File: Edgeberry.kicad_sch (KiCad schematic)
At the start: 27 parts, among them P1 12Vin, Q1 BC547, Q2 BC547, Q3 BC547, SW1 SW_PUSH, U1 24LC256, U2 LM2596S-5.0

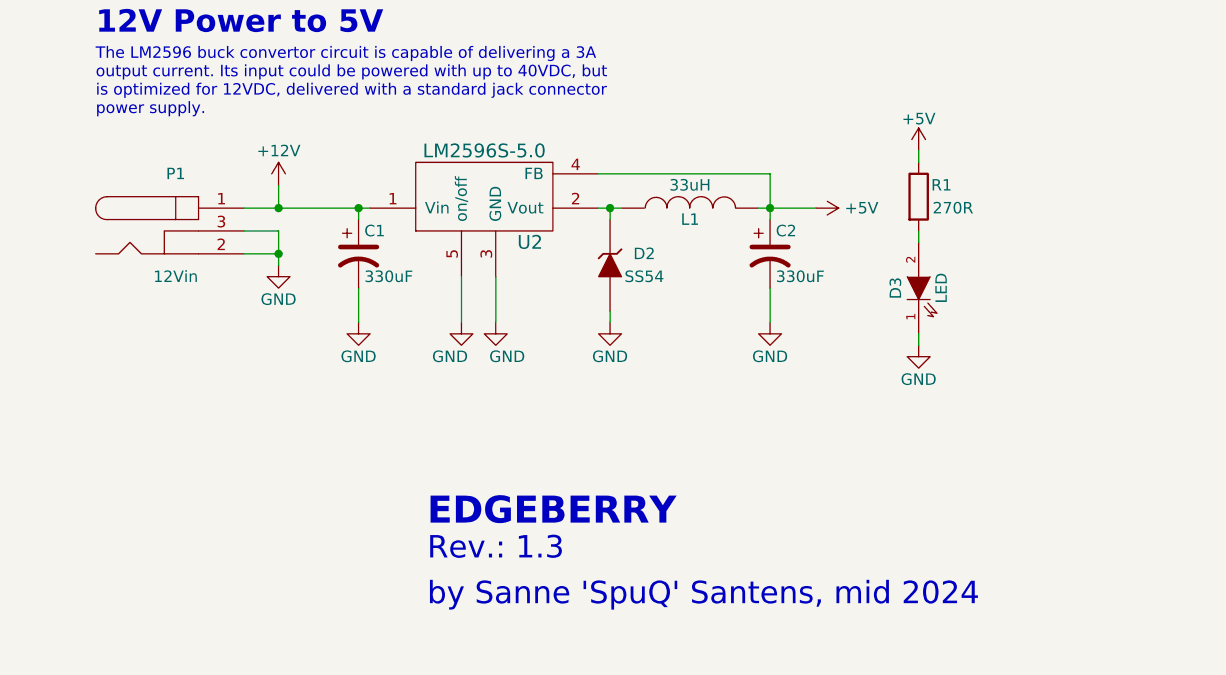
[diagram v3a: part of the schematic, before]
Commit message: Added a Molex 2Pin header on 12V
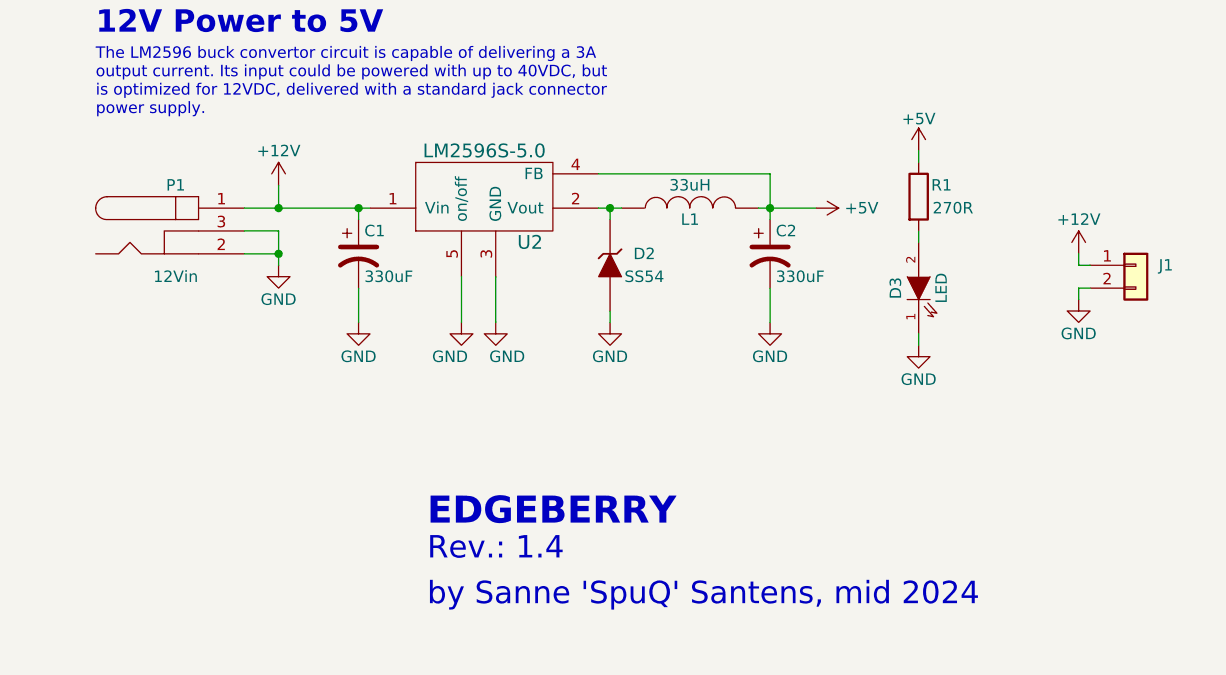
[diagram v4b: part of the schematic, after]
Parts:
- added J1: Molex_KK_1x02_P2.54mm, Connector_Molex:Molex_KK-254_AE-6410-02A_1x02_P2.54mm_Vertical, symbol Connector_Generic:Conn_01x02
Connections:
- net +12V: now also J1.1 (Pin_1)
- net GND: now also J1.2 (Pin_2)
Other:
- note added: "Rev.: 1.4"
- note removed: "Rev.: 1.3"
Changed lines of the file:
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@@
     (title "Edgeberry Hardware")
     (date "2024-05-15")
-    (rev "1.3")
+    (rev "1.4")
   )
   (junction (at 91.44 149.86) (diameter 0) (color 0 0 0 0)
@@
     (stroke (width 0) (type default) (color 0 0 0 0))
   )
+  (wire (pts (xy 255.27 142.24) (xy 254 142.24))
+    (stroke (width 0) (type default) (color 0 0 0 0))
+  )
   (wire (pts (xy 58.42 148.59) (xy 58.42 149.86))
     (stroke (width 0) (type default) (color 0 0 0 0))
@@
     (stroke (width 0) (type default) (color 0 0 0 0))
   )
+  (wire (pts (xy 254 144.78) (xy 254 146.05))
+    (stroke (width 0) (type default) (color 0 0 0 0))
+  )
   (wire (pts (xy 130.81 39.37) (xy 133.35 39.37))
     (stroke (width 0) (type default) (color 0 0 0 0))
@@
     (stroke (width 0) (type default) (color 0 0 0 0))
   )
+  (wire (pts (xy 255.27 144.78) (xy 254 144.78))
+    (stroke (width 0) (type default) (color 0 0 0 0))
+  )
   (wire (pts (xy 201.93 135.89) (xy 203.2 135.89))
     (stroke (width 0) (type default) (color 0 0 0 0))
@@
   )
   (wire (pts (xy 130.81 64.77) (xy 133.35 64.77))
+    (stroke (width 0) (type default) (color 0 0 0 0))
+  )
+  (wire (pts (xy 254 142.24) (xy 254 140.97))
     (stroke (width 0) (type default) (color 0 0 0 0))
   )
@@
     (effects (font (size 1.27 1.27)) (justify left bottom))
   )
-  (text "Rev.: 1.3" (at 181.61 175.26 0)
+  (text "Rev.: 1.4" (at 181.61 175.26 0)
     (effects (font (size 2.4892 2.4892)) (justify left bottom))
   )
@@
   (symbol (lib_id "EdgeBerry-rescue:BARREL_JACK") (at 153.67 138.43 0) (unit 1)
     (in_bom yes) (on_board yes)
-    (property "Reference" "P1" (id 0) (at 153.67 132.08 0))
+    (property "Reference" "P1" (id 0) (at 153.67 133.35 0))
     (property "Value" "12Vin" (id 1) (at 153.67 143.51 0))
     (property "Footprint" "Connector_BarrelJack:BarrelJack_Horizontal" (id 2) (at 153.67 138.43 0)
@@
     (pin "1")
   )
+  (symbol (lib_id "power:+12V") (at 254 140.97 0) (unit 1)
+    (in_bom yes) (on_board yes)
+    (property "Reference" "#PWR0106" (id 0) (at 254 144.78 0)
+      (effects (font (size 1.27 1.27)) hide)
+    )
+    (property "Value" "+12V" (id 1) (at 254 137.16 0))
+    (property "Footprint" "" (id 2) (at 254 140.97 0)
+      (effects (font (size 1.27 1.27)) hide)
+    )
+    (property "Datasheet" "" (id 3) (at 254 140.97 0)
+      (effects (font (size 1.27 1.27)) hide)
+    )
+    (pin "1")
+  )
   (symbol (lib_id "EdgeBerry-rescue:+3V3") (at 130.81 34.29 90) (unit 1)
     (in_bom yes) (on_board yes)
-    (property "Reference" "#PWR?" (id 0) (at 134.62 34.29 0)
+    (property "Reference" "#PWR0107" (id 0) (at 134.62 34.29 0)
       (effects (font (size 1.27 1.27)) hide)
     )
@@
     (pin "1")
   )
+  (symbol (lib_id "Connector_Generic:Conn_01x02") (at 260.35 142.24 0) (unit 1)
+    (in_bom yes) (on_board yes)
+    (property "Reference" "J1" (id 0) (at 262.89 142.2399 0)
+      (effects (font (size 1.27 1.27)) (justify left))
+    )
+    (property "Value" "Molex_KK_1x02_P2.54mm" (id 1) (at 256.54 147.32 0)
+      (effects (font (size 1.27 1.27)) (justify left) hide)
+    )
+    (property "Footprint" "Connector_Molex:Molex_KK-254_AE-6410-02A_1x02_P2.54mm_Vertical" (id 2) (at 260.35 142.24 0)
+      (effects (font (size 1.27 1.27)) hide)
+    )
+    (property "Datasheet" "~" (id 3) (at 260.35 142.24 0)
+      (effects (font (size 1.27 1.27)) hide)
+    )
+    (pin "1")
+    (pin "2")
+  )
   (symbol (lib_id "power:+5V") (at 54.61 29.21 0) (unit 1)
     (in_bom yes) (on_board yes)
@@
     (pin "2")
   )
+  (symbol (lib_id "power:GND") (at 254 146.05 0) (unit 1)
+    (in_bom yes) (on_board yes)
+    (property "Reference" "#PWR0105" (id 0) (at 254 152.4 0)
+      (effects (font (size 1.27 1.27)) hide)
+    )
+    (property "Value" "GND" (id 1) (at 254 149.86 0))
+    (property "Footprint" "" (id 2) (at 254 146.05 0)
+      (effects (font (size 1.27 1.27)) hide)
+    )
+    (property "Datasheet" "" (id 3) (at 254 146.05 0)
+      (effects (font (size 1.27 1.27)) hide)
+    )
+    (pin "1")
+  )
   (sheet_instances
     (path "/" (page "1"))
@@
       (reference "#PWR0103") (unit 1) (value "+5V") (footprint "")
     )
-    (path "/1eae0866-fb43-460e-ba70-4206816f3ae0"
+    (path "/1eae0866-fb43-460e-ba70-4206816f3ae1"
       (reference "#PWR0104") (unit 1) (value "+5V") (footprint "")
     )
+    (path "/f44cc862-d425-4144-8846-d84278a3c917"
+      (reference "#PWR0105") (unit 1) (value "GND") (footprint "")
+    )
+    (path "/2623d6cf-f221-488b-8577-990bdece26e9"
+      (reference "#PWR0106") (unit 1) (value "+12V") (footprint "")
+    )
     (path "/59ba752a-b2a2-4535-9bd8-a06a7b8b7a31"
-      (reference "#PWR?") (unit 1) (value "+3V3") (footprint "")
+      (reference "#PWR0107") (unit 1) (value "+3V3") (footprint "")
     )
     (path "/00000000-0000-0000-0000-00005b755152"
@@
       (reference "H1") (unit 1) (value "EdgeBerry_IO") (footprint "emcosys:EdgeBerry_IO")
     )
+    (path "/8a9dd820-4ec5-4959-94a2-489c1e5fdf0f"
+      (reference "J1") (unit 1) (value "Molex_KK_1x02_P2.54mm") (footprint "Connector_Molex:Molex_KK-254_AE-6410-02A_1x02_P2.54mm_Vertical")
+    )
     (path "/0a17adb6-bec6-42e3-96c1-992b250e6557"

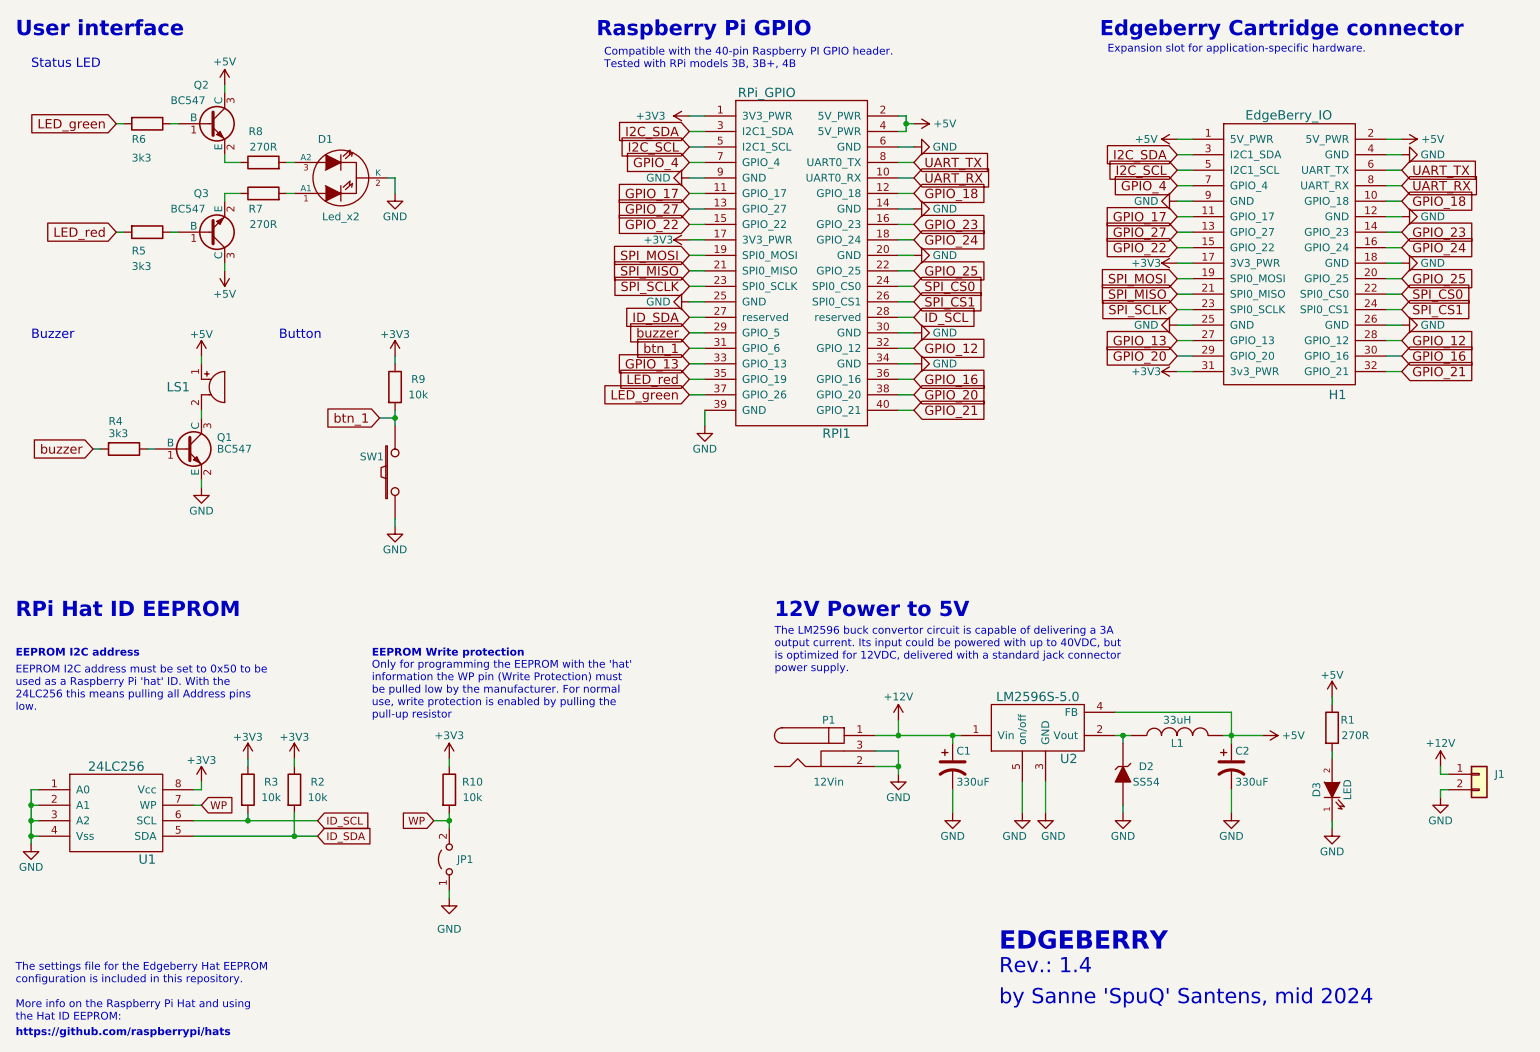
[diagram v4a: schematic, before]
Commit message: Bugfix RPi footprint + via's are via's now instead footprints. KiCad * update.
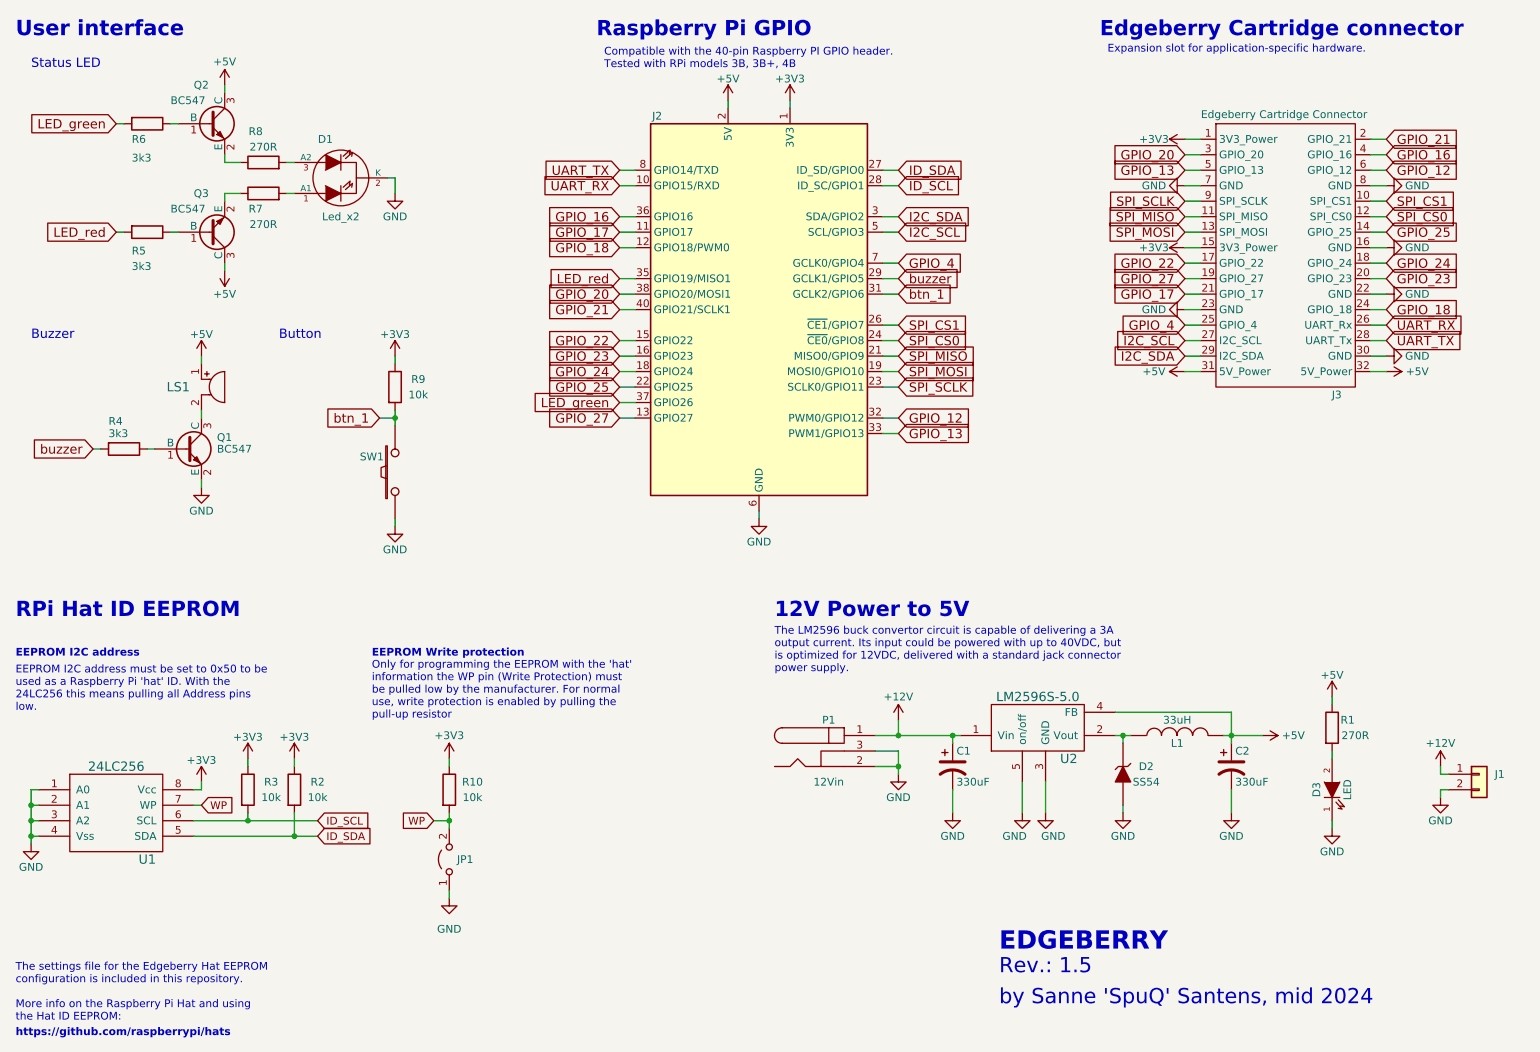
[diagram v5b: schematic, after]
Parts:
- removed H1: EdgeBerry_IO, emcosys:EdgeBerry_IO, symbol EdgeBerry-rescue:EdgeBerry_IO
- removed RPI1: RPi_GPIO, emcosys:RPI_GPIO, symbol EdgeBerry-rescue:RPi_GPIO
- added J2: Raspberry_Pi_2_3, Connector_PinSocket_2.54mm:PinSocket_2x20_P2.54mm_Vertical, symbol Connector:Raspberry_Pi_2_3
- added J3: Edgeberry Cartridge Connector, Connector_PinSocket_2.54mm:PinSocket_2x16_P2.54mm_Horizontal, symbol Edgeberry:Edgeberry_Cartridge_Connector
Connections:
- net +3V3: now also J2.1 (3V3), J2.17 (3V3), J3.1 (3V3_Power), J3.15 (3V3_Power)
- net +5V: now also J2.2 (5V), J2.4 (5V), J3.31 (5V_Power), J3.32 (5V_Power)
- net GND: now also J2.14 (GND), J2.20 (GND), J2.25 (GND), J2.30 (GND), J2.34 (GND), J2.39 (GND), J2.6 (GND), J2.9 (GND), J3.16 (GND), J3.22 (GND), J3.23 (GND), J3.30 (GND), J3.7 (GND), J3.8 (GND)
- net GPIO_12: now also J2.32 (PWM0/GPIO12), J3.6 (GPIO_12)
- net GPIO_13: now also J2.33 (PWM1/GPIO13), J3.5 (GPIO_13)
- net GPIO_16: now also J2.36 (GPIO16), J3.4 (GPIO_16)
- net GPIO_17: now also J2.11 (GPIO17), J3.21 (GPIO_17)
- net GPIO_18: now also J2.12 (GPIO18/PWM0), J3.24 (GPIO_18)
- net GPIO_20: now also J2.38 (GPIO20/MOSI1), J3.3 (GPIO_20)
- net GPIO_21: now also J2.40 (GPIO21/SCLK1), J3.2 (GPIO_21)
- net GPIO_22: now also J2.15 (GPIO22), J3.17 (GPIO_22)
- net GPIO_23: now also J2.16 (GPIO23), J3.20 (GPIO_23)
- net GPIO_24: now also J2.18 (GPIO24), J3.18 (GPIO_24)
- net GPIO_25: now also J2.22 (GPIO25), J3.14 (GPIO_25)
- net GPIO_27: now also J2.13 (GPIO27), J3.19 (GPIO_27)
- net GPIO_4: now also J2.7 (GCLK0/GPIO4), J3.25 (GPIO_4)
- net I2C_SCL: now also J2.5 (SCL/GPIO3), J3.27 (I2C_SCL)
- net I2C_SDA: now also J2.3 (SDA/GPIO2), J3.29 (I2C_SDA)
- net ID_SCL: now also J2.28 (ID_SC/GPIO1)
- net ID_SDA: now also J2.27 (ID_SD/GPIO0)
- net LED_green: now also J2.37 (GPIO26)
- net LED_red: now also J2.35 (GPIO19/MISO1)
- net SPI_CS0: now also J2.24 (~{CE0}/GPIO8), J3.12 (SPI_CS0)
- net SPI_CS1: now also J2.26 (~{CE1}/GPIO7), J3.10 (SPI_CS1)
- net SPI_MISO: now also J2.21 (MISO0/GPIO9), J3.11 (SPI_MISO)
- net SPI_MOSI: now also J2.19 (MOSI0/GPIO10), J3.13 (SPI_MOSI)
- net SPI_SCLK: now also J2.23 (SCLK0/GPIO11), J3.9 (SPI_SCLK)
- net UART_RX: now also J2.10 (GPIO15/RXD), J3.26 (UART_Rx)
- net UART_TX: now also J2.8 (GPIO14/TXD), J3.28 (UART_Tx)
- net btn_1: now also J2.31 (GCLK2/GPIO6)
- net buzzer: now also J2.29 (GCLK1/GPIO5)
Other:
- note added: "Rev.: 1.5"
- note removed: "Rev.: 1.4"
